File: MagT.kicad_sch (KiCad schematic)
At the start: 9 parts, among them IC1 DRV8212DSGR, IC2 DRV8212DSGR, IC3 DRV8212DSGR

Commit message: Update some part numbers
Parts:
- IC1, IC2, IC3: Part Number (none) -> DRV8212DSGR
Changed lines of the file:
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@@
+      (effects (font (size 1.27 1.27)) hide)
+    )
+    (property "Part Number" "DRV8212DSGR" (at 67.31 96.52 0)
       (effects (font (size 1.27 1.27)) hide)
     )
@@
       (effects (font (size 1.27 1.27)) hide)
     )
+    (property "Part Number" "DRV8212DSGR" (at 67.31 135.89 0)
+      (effects (font (size 1.27 1.27)) hide)
+    )
     (pin "1")
     (pin "2")
@@
       (effects (font (size 1.27 1.27)) hide)
     )
+    (property "Part Number" "DRV8212DSGR" (at 67.31 54.61 0)
+      (effects (font (size 1.27 1.27)) hide)
+    )

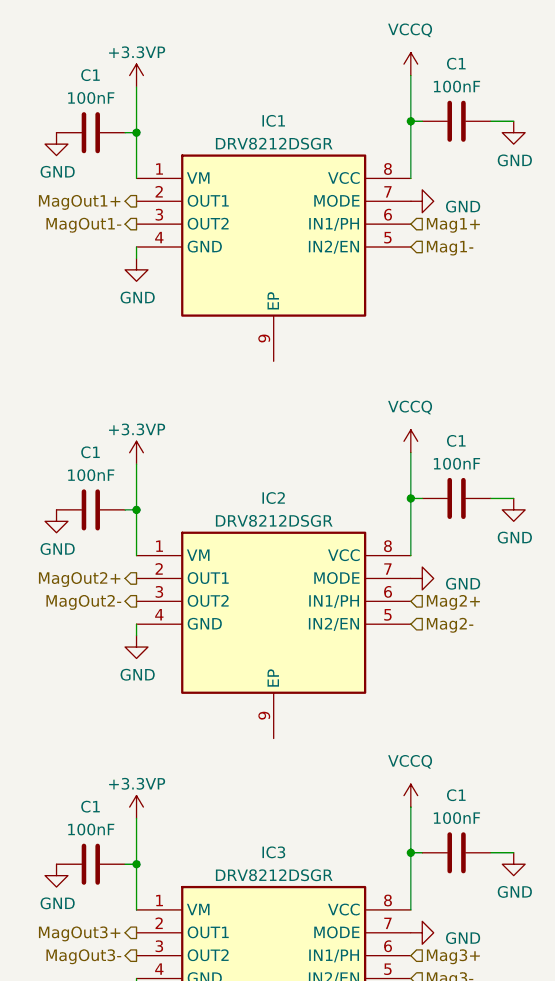
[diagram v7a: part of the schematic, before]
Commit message: Update project to kicad 8
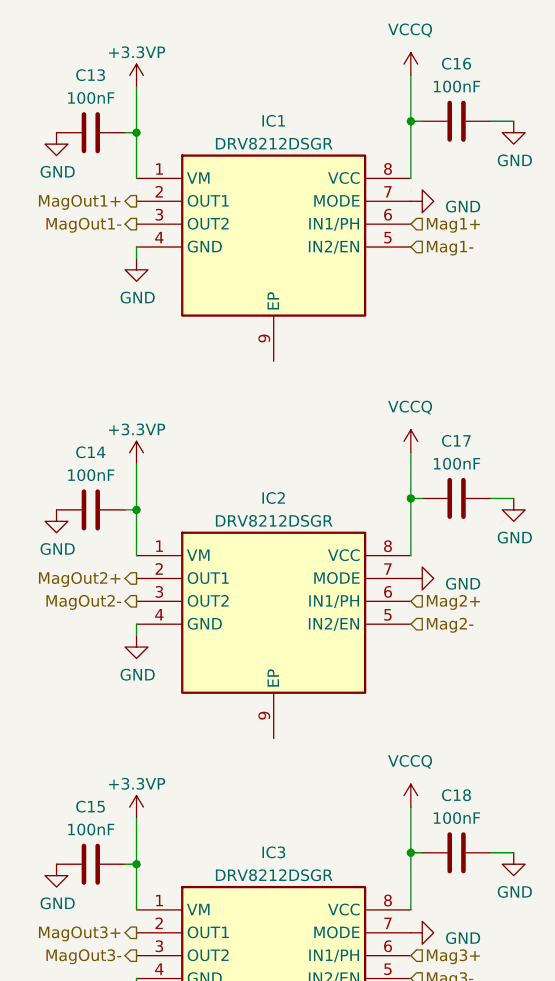
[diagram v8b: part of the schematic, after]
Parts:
- renumbered C1 to C13, C1 to C14, C1 to C15, C1 to C16, C1 to C17, C1 to C18
